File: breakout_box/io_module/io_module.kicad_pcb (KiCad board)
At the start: 2 copper layers, 53.8 x 35 mm, 6 parts, among them J1 ZHEJINAG_CK_STSJACKS, J2 ZHEJINAG_CK_STSJACKS, J3 ZHEJINAG_CK_STSJACKS

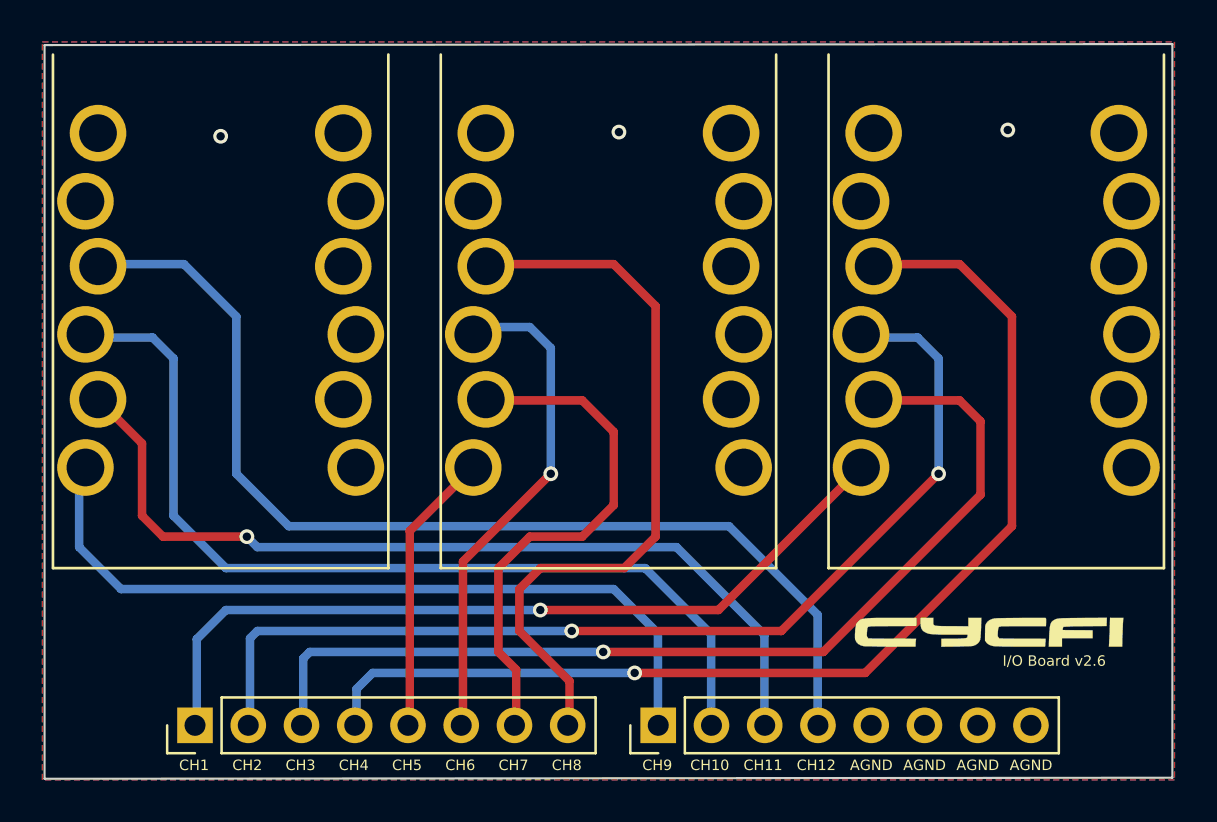
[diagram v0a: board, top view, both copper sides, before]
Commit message: io_module fab updates; update to latest kicad
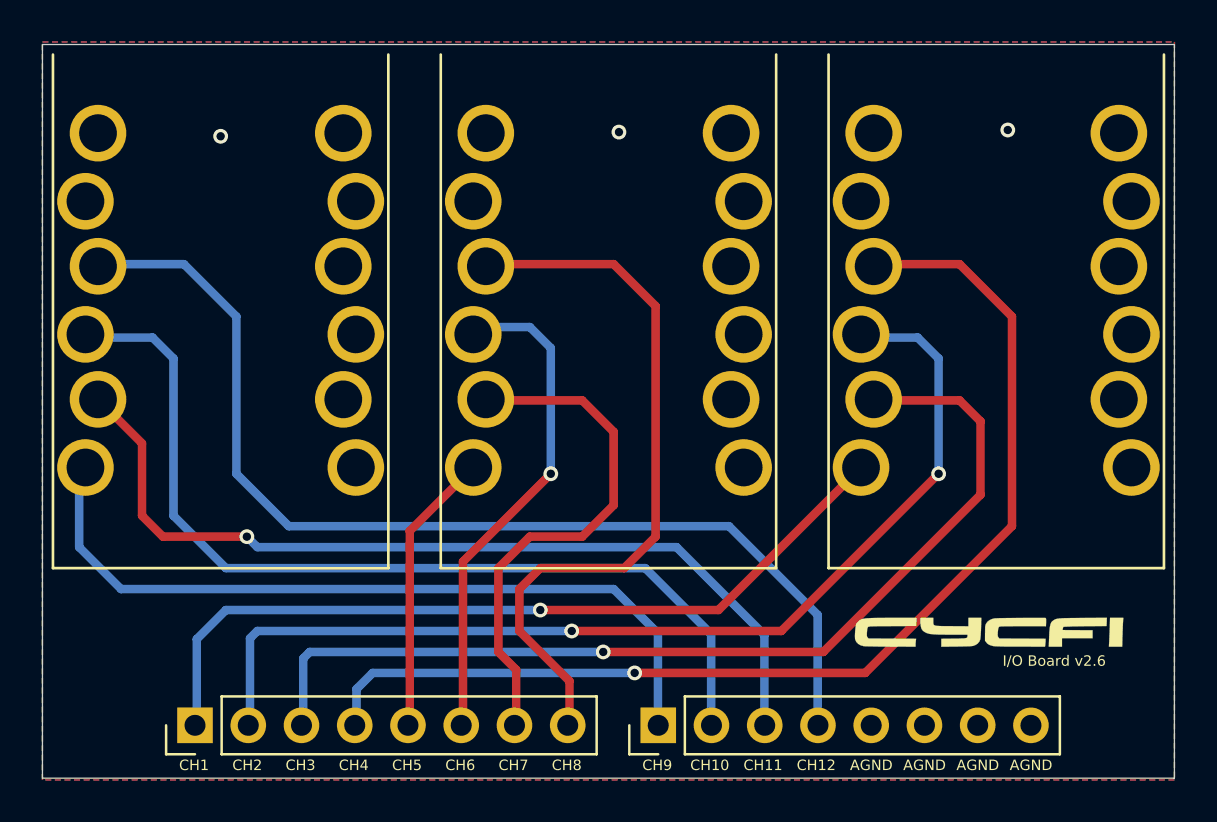
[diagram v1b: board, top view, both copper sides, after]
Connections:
- net GND renamed AGND
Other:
- board size 53.8 x 35 mm -> 54 x 35 mm
